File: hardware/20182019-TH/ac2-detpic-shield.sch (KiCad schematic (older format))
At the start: 46 parts, among them J1 HEADER, J2 HEADER, J3 HEADER, J4 HEADER, J5 HEADER, J6 HEADER, J7 HEADER, Q1 VN2222, Q2 VN2222, SW1 SW_DIP_x04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

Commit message: fixed bug in J3 header in 20182019-TH pcb
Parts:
- removed J3: HEADER, Connector_PinHeader_2.54mm:PinHeader_1x07_P2.54mm_Vertical, symbol Connector:Conn_01x07_Male
- added J3: HEADER, Connector_PinHeader_2.54mm:PinHeader_1x06_P2.54mm_Vertical, symbol Connector:Conn_01x06_Male
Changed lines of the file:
@@
 Text Label 1450 2950 0    50   ~ 10
 RD0
-Text Label 1450 3150 0    50   ~ 10
+Text Label 1550 3150 0    50   ~ 10
 RD10
 Text Label 1600 3250 0    50   ~ 10
@@
 $EndComp
 $Comp
-L Connector:Conn_01x07_Male J3
-U 1 1 5C9D88C9
-P 1750 2850
-F 0 "J3" H 1650 2850 50  0000 R CNN
-F 1 "HEADER" V 1700 3000 50  0000 R CNN
-F 2 "Connector_PinHeader_2.54mm:PinHeader_1x07_P2.54mm_Vertical" H 1750 2850 50  0001 C CNN
-F 3 "~" H 1750 2850 50  0001 C CNN
-	1    1750 2850
-	-1   0    0    1
-$EndComp
-$Comp
 L Connector:Conn_01x02_Male J4
 U 1 1 5C9DA65B
@@
 	1550 3050 1450 3050
 Wire Wire Line
-	1550 3150 1450 3150
-Wire Wire Line
 	1550 3350 1450 3350
 Wire Wire Line
@@
 Text Notes 10570 7640 0    50   ~ 10
 v1.1 May 2019
+$Comp
+L Connector:Conn_01x06_Male J3
+U 1 1 5CF092BF
+P 1750 2850
+F 0 "J3" H 1650 2800 50  0000 R CNN
+F 1 "HEADER" V 1700 2950 50  0000 R CNN
+F 2 "Connector_PinHeader_2.54mm:PinHeader_1x06_P2.54mm_Vertical" H 1750 2850 50  0001 C CNN
+F 3 "~" H 1750 2850 50  0001 C CNN
+	1    1750 2850
+	-1   0    0    1
+$EndComp
+Wire Wire Line
+	1450 3150 1750 3150
 $EndSCHEMATC

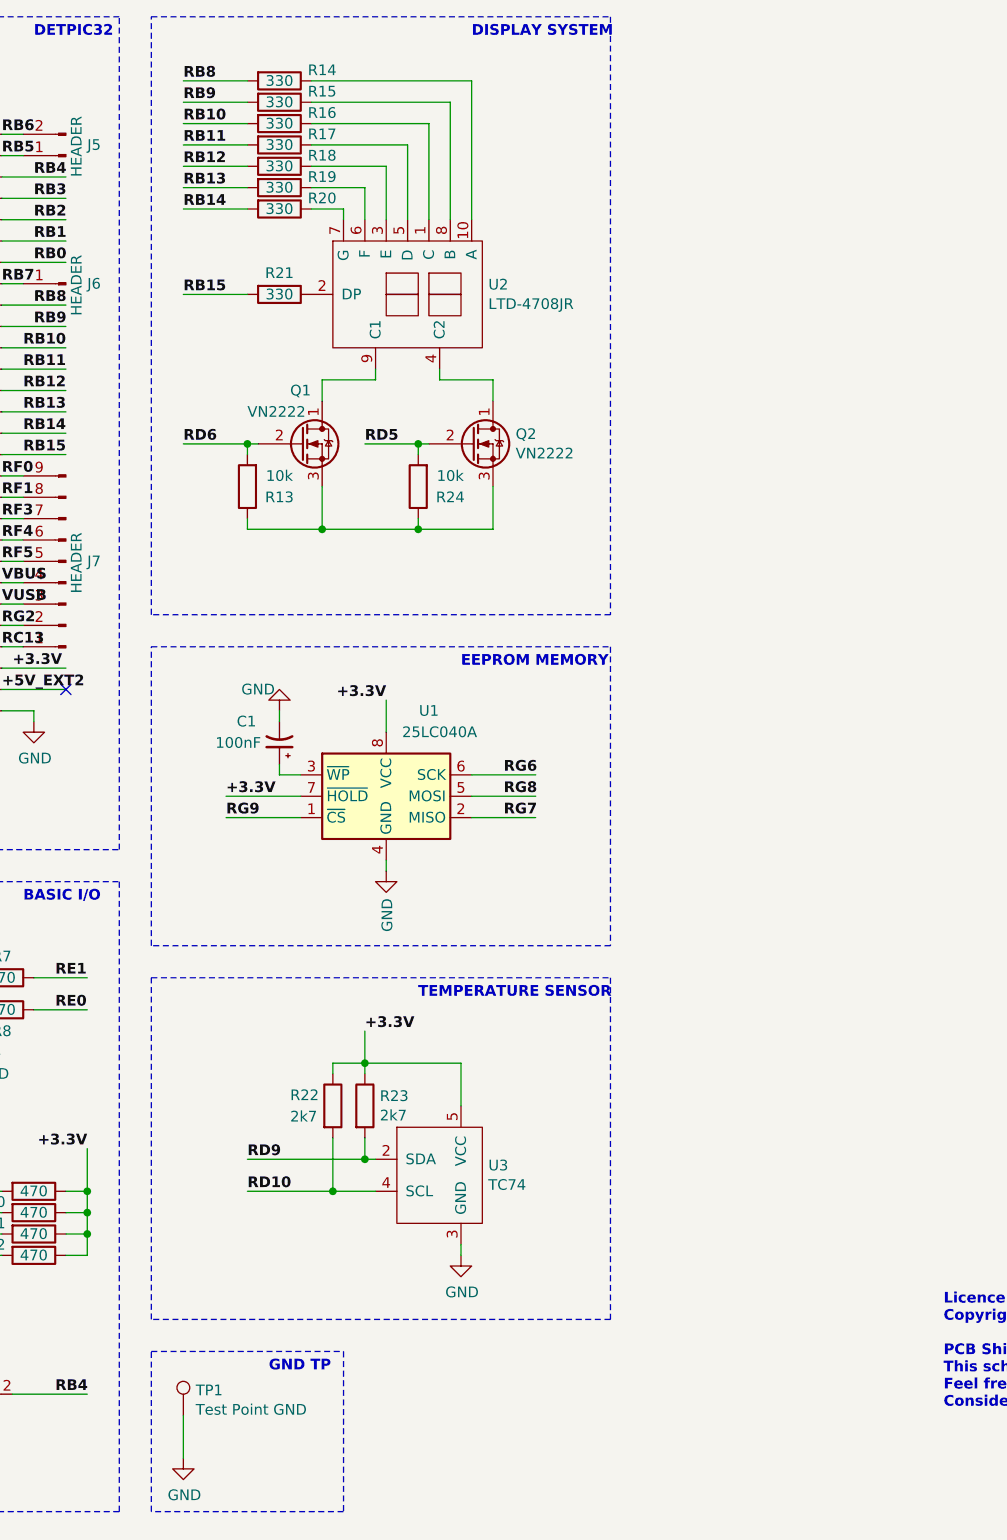
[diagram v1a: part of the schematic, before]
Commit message: rotary pot, option on dual single 7seg displays and fix in trim pot
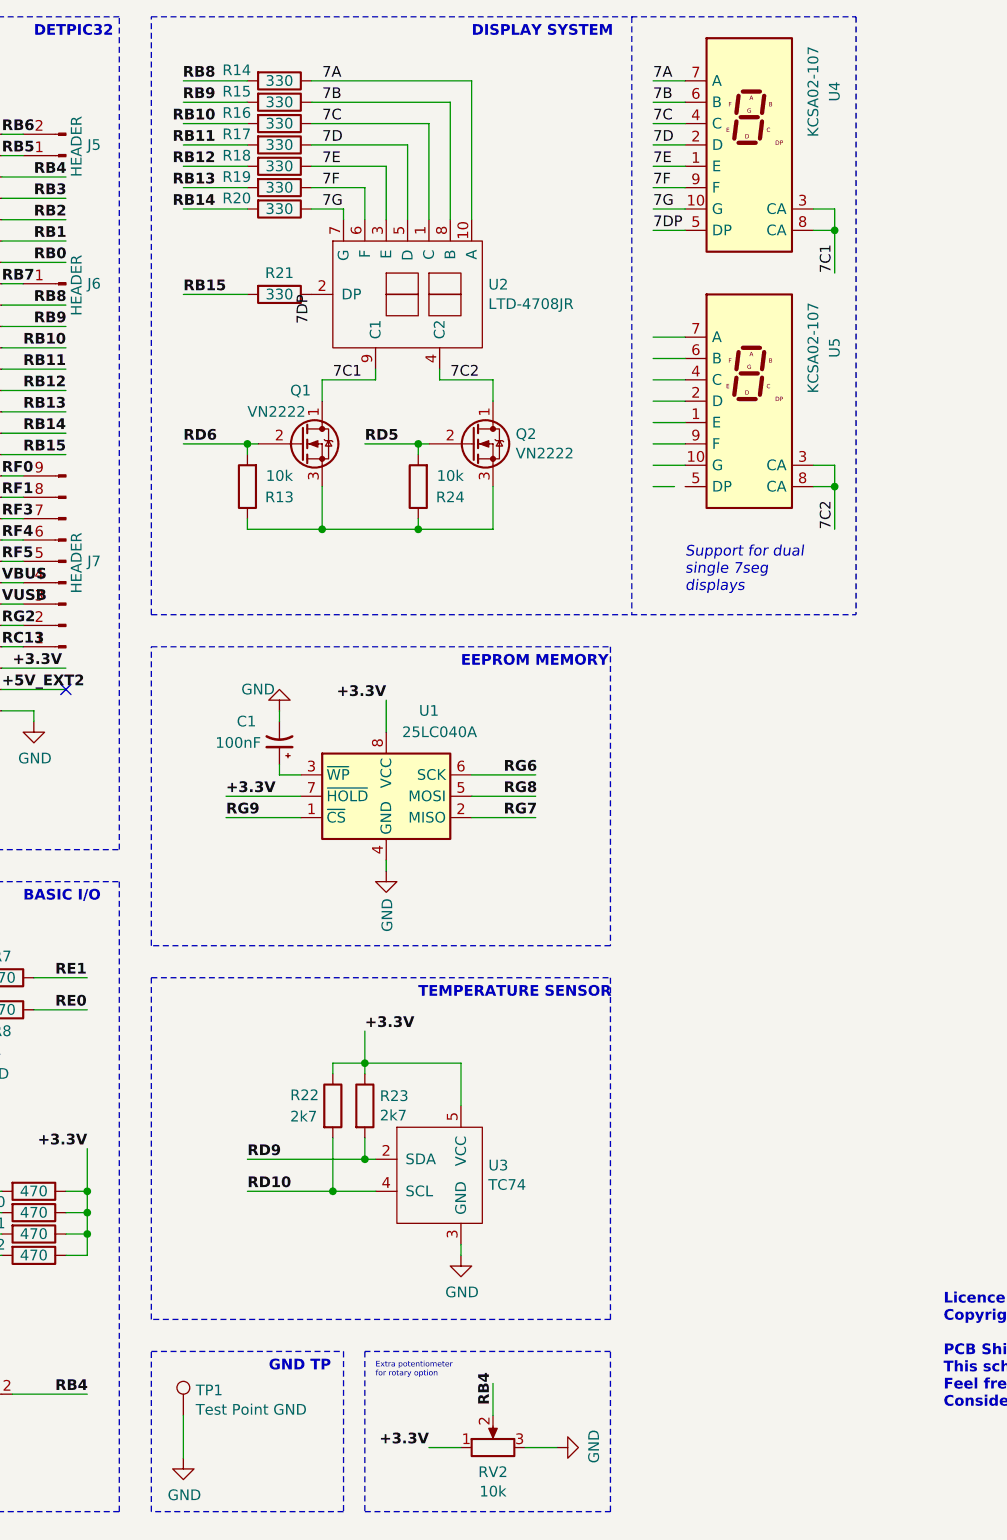
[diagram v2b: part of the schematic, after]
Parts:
- added RV2: 10k, Potentiometer_THT:Potentiometer_Piher_T-16H_Single_Horizontal, symbol Device:R_POT
- added U4, U5: KCSA02-107, Display_7Segment:7SegmentLED_LTS6760_LTS6780, symbol Display_Character:KCSA02-107
- RV1: footprint Potentiometer_THT:Potentiometer_ACP_CA14V-15_Vertical -> Potentiometer_THT:Potentiometer_ACP_CA9-V10_Vertical
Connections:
- net labels added: 7A, 7B, 7C, 7C1, 7C2, 7D, 7DP, 7E, 7F, 7G
- wire segments 172 -> 199
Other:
- note added: "Extra potentiometer\nfor rotary option"
- note added: "Support for dual \nsingle 7seg\ndisplays"
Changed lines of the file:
@@
 Wire Wire Line
 	3750 1500 3450 1500
-Text Label 3450 900  0    50   ~ 10
+Text Label 3600 900  2    50   ~ 10
 RB8
-Text Label 3450 1000 0    50   ~ 10
+Text Label 3600 1000 2    50   ~ 10
 RB9
-Text Label 3450 1100 0    50   ~ 10
+Text Label 3600 1100 2    50   ~ 10
 RB10
-Text Label 3450 1200 0    50   ~ 10
+Text Label 3600 1200 2    50   ~ 10
 RB11
-Text Label 3450 1300 0    50   ~ 10
+Text Label 3600 1300 2    50   ~ 10
 RB12
-Text Label 3450 1400 0    50   ~ 10
+Text Label 3600 1400 2    50   ~ 10
 RB13
-Text Label 3450 1500 0    50   ~ 10
+Text Label 3600 1500 2    50   ~ 10
 RB14
 $Comp
@@
 	4800 900  4800 1550
 Wire Wire Line
-	3750 1900 3450 1900
-Text Label 3450 1900 0    50   ~ 10
-RB15
-Wire Wire Line
 	4350 2250 4350 2300
 Wire Wire Line
@@
 	4550 2600 4300 2600
 Wire Notes Line
-	3300 600  5450 600
-Wire Notes Line
-	5450 600  5450 3400
-Wire Notes Line
-	5450 3400 3300 3400
+	5550 600  5550 3400
 Wire Notes Line
 	3300 3400 3300 600
@@
 F 0 "RV1" H 2430 7096 50  0000 R CNN
 F 1 "10k" H 2430 7005 50  0000 R CNN
-F 2 "Potentiometer_THT:Potentiometer_ACP_CA14V-15_Vertical" H 2500 7050 50  0001 C CNN
+F 2 "Potentiometer_THT:Potentiometer_ACP_CA9-V10_Vertical" H 2500 7050 50  0001 C CNN
 F 3 "~" H 2500 7050 50  0001 C CNN
 	1    2500 7050
@@
 U 1 1 5CA1D1A8
 P 3900 900
-F 0 "R14" V 3850 1100 50  0000 C CNN
+F 0 "R14" V 3850 700 50  0000 C CNN
 F 1 "330" V 3900 900 50  0000 C CNN
 F 2 "Resistor_THT:R_Axial_DIN0207_L6.3mm_D2.5mm_P7.62mm_Horizontal" V 3830 900 50  0001 C CNN
@@
 U 1 1 5CA1F029
 P 3900 1000
-F 0 "R15" V 3850 1200 50  0000 C CNN
+F 0 "R15" V 3850 800 50  0000 C CNN
 F 1 "330" V 3900 1000 50  0000 C CNN
 F 2 "Resistor_THT:R_Axial_DIN0207_L6.3mm_D2.5mm_P7.62mm_Horizontal" V 3830 1000 50  0001 C CNN
@@
 U 1 1 5CA25E86
 P 3900 1100
-F 0 "R16" V 3850 1300 50  0000 C CNN
+F 0 "R16" V 3850 900 50  0000 C CNN
 F 1 "330" V 3900 1100 50  0000 C CNN
 F 2 "Resistor_THT:R_Axial_DIN0207_L6.3mm_D2.5mm_P7.62mm_Horizontal" V 3830 1100 50  0001 C CNN
@@
 U 1 1 5CA2CC58
 P 3900 1200
-F 0 "R17" V 3850 1400 50  0000 C CNN
+F 0 "R17" V 3850 1000 50  0000 C CNN
 F 1 "330" V 3900 1200 50  0000 C CNN
 F 2 "Resistor_THT:R_Axial_DIN0207_L6.3mm_D2.5mm_P7.62mm_Horizontal" V 3830 1200 50  0001 C CNN
@@
 U 1 1 5CA33A2A
 P 3900 1300
-F 0 "R18" V 3850 1500 50  0000 C CNN
+F 0 "R18" V 3850 1100 50  0000 C CNN
 F 1 "330" V 3900 1300 50  0000 C CNN
 F 2 "Resistor_THT:R_Axial_DIN0207_L6.3mm_D2.5mm_P7.62mm_Horizontal" V 3830 1300 50  0001 C CNN
@@
 U 1 1 5CA41AE3
 P 3900 1400
-F 0 "R19" V 3850 1600 50  0000 C CNN
+F 0 "R19" V 3850 1200 50  0000 C CNN
 F 1 "330" V 3900 1400 50  0000 C CNN
 F 2 "Resistor_THT:R_Axial_DIN0207_L6.3mm_D2.5mm_P7.62mm_Horizontal" V 3830 1400 50  0001 C CNN
@@
 U 1 1 5CA488AB
 P 3900 1500
-F 0 "R20" V 3850 1700 50  0000 C CNN
+F 0 "R20" V 3850 1300 50  0000 C CNN
 F 1 "330" V 3900 1500 50  0000 C CNN
 F 2 "Resistor_THT:R_Axial_DIN0207_L6.3mm_D2.5mm_P7.62mm_Horizontal" V 3830 1500 50  0001 C CNN
@@
 	4100 3000 4550 3000
 $Comp
-L Device:R R21
-U 1 1 5CA72E7A
-P 3900 1900
-F 0 "R21" V 3800 1900 50  0000 C CNN
-F 1 "330" V 3900 1900 50  0000 C CNN
-F 2 "Resistor_THT:R_Axial_DIN0207_L6.3mm_D2.5mm_P7.62mm_Horizontal" V 3830 1900 50  0001 C CNN
-F 3 "~" H 3900 1900 50  0001 C CNN
-	1    3900 1900
-	0    1    1    0
-$EndComp
-$Comp
 L Memory_EEPROM:25LCxxx U1
 U 1 1 5C985584
@@
 Wire Wire Line
 	1450 3150 1750 3150
+$Comp
+L Display_Character:KCSA02-107 U4
+U 1 1 5E60EA09
+P 6100 1200
+F 0 "U4" V 6500 1450 50  0000 C CNN
+F 1 "KCSA02-107" V 6400 1450 50  0000 C CNN
+F 2 "Display_7Segment:7SegmentLED_LTS6760_LTS6780" H 6100 600 50  0001 C CNN
+F 3 "http://www.kingbright.com/attachments/file/psearch/000/00/00/KCSA02-107(Ver.10A).pdf" H 5600 1675 50  0001 L CNN
+	1    6100 1200
+	1    0    0    -1
+$EndComp
+$Comp
+L Display_Character:KCSA02-107 U5
+U 1 1 5E63DD93
+P 6100 2400
+F 0 "U5" V 6500 2650 50  0000 C CNN
+F 1 "KCSA02-107" V 6400 2650 50  0000 C CNN
+F 2 "Display_7Segment:7SegmentLED_LTS6760_LTS6780" H 6100 1800 50  0001 C CNN
+F 3 "http://www.kingbright.com/attachments/file/psearch/000/00/00/KCSA02-107(Ver.10A).pdf" H 5600 2875 50  0001 L CNN
+	1    6100 2400
+	1    0    0    -1
+$EndComp
+Wire Notes Line
+	6600 600  6600 3400
+Wire Notes Line
+	3300 600  6600 600
+Wire Notes Line
+	3300 3400 6600 3400
+Text Notes 5800 3300 0    50   Italic 0
+Support for dual \nsingle 7seg\ndisplays
+Text Label 4100 1500 0    50   ~ 0
+7G
+Text Label 4100 1400 0    50   ~ 0
+7F
+Text Label 4100 1300 0    50   ~ 0
+7E
+Text Label 4100 1200 0    50   ~ 0
+7D
+Text Label 4100 1100 0    50   ~ 0
+7C
+Text Label 4100 1000 0    50   ~ 0
+7B
+Text Label 4100 900  0    50   ~ 0
+7A
+Wire Wire Line
+	3750 1900 3450 1900
+Text Label 3450 1900 0    50   ~ 10
+RB15
+$Comp
+L Device:R R21
+U 1 1 5CA72E7A
+P 3900 1900
+F 0 "R21" V 3800 1900 50  0000 C CNN
+F 1 "330" V 3900 1900 50  0000 C CNN
+F 2 "Resistor_THT:R_Axial_DIN0207_L6.3mm_D2.5mm_P7.62mm_Horizontal" V 3830 1900 50  0001 C CNN
+F 3 "~" H 3900 1900 50  0001 C CNN
+	1    3900 1900
+	0    1    1    0
+$EndComp
+Text Label 4050 1900 3    50   ~ 0
+7DP
+Text Label 4150 2300 0    50   ~ 0
+7C1
+Text Label 4700 2300 0    50   ~ 0
+7C2
+Wire Wire Line
+	5800 1000 5650 1000
+Wire Wire Line
+	5800 900  5650 900
+Wire Wire Line
+	5800 1100 5650 1100
+Wire Wire Line
+	5800 1200 5650 1200
+Wire Wire Line
+	5800 1300 5650 1300
+Wire Wire Line
+	5800 1400 5650 1400
+Wire Wire Line
+	5800 1500 5650 1500
+Wire Wire Line
+	5800 1600 5650 1600
+Wire Wire Line
+	6400 1500 6500 1500
+Wire Wire Line
+	6500 1500 6500 1600
+Wire Wire Line
+	6400 1600 6500 1600
+Connection ~ 6500 1600
+Wire Wire Line
+	6500 1600 6500 1800
+Wire Wire Line
+	5800 2100 5650 2100
+Wire Wire Line
+	5800 2200 5650 2200
+Wire Wire Line
+	5800 2300 5650 2300
+Wire Wire Line
+	5800 2400 5650 2400
+Wire Wire Line
+	5800 2500 5650 2500
+Wire Wire Line
+	5800 2600 5650 2600
+Wire Wire Line
+	5800 2700 5650 2700
+Wire Wire Line
+	5750 2800 5650 2800
+Wire Wire Line
+	6400 2700 6500 2700
+Wire Wire Line
+	6500 2700 6500 2800
+Wire Wire Line
+	6400 2800 6500 2800
+Connection ~ 6500 2800
+Wire Wire Line
+	6500 2800 6500 3000
+Text Label 5650 900  0    50   ~ 0
+7A
+Text Label 5650 1000 0    50   ~ 0
+7B
+Text Label 5650 1100 0    50   ~ 0
+7C
+Text Label 5650 1200 0    50   ~ 0
+7D
+Text Label 5650 1300 0    50   ~ 0
+7E
+Text Label 5650 1400 0    50   ~ 0
+7F
+Text Label 5650 1500 0    50   ~ 0
+7G
+Text Label 5650 1600 0    50   ~ 0
+7DP
+Text Label 6500 1800 1    50   ~ 0
+7C1
+Text Label 6500 3000 1    50   ~ 0
+7C2
+$Comp
+L Device:R_POT RV2
+U 1 1 5E854091
+P 4900 7300
+F 0 "RV2" V 4785 7300 50  0000 C CNN
+F 1 "10k" V 4694 7300 50  0000 C CNN
+F 2 "Potentiometer_THT:Potentiometer_Piher_T-16H_Single_Horizontal" H 4900 7300 50  0001 C CNN
+F 3 "~" H 4900 7300 50  0001 C CNN
+	1    4900 7300
+	0    -1   -1   0
+$EndComp
+Wire Wire Line
+	4900 7150 4900 7000
+Wire Wire Line
+	5050 7300 5200 7300
+Wire Wire Line
+	4750 7300 4600 7300
+Text Label 4900 7100 1    50   ~ 10
+RB4
+$Comp
+L power:GND #PWR05
+U 1 1 5E87CB07
+P 5200 7300
+F 0 "#PWR05" H 5200 7050 50  0001 C CNN
+F 1 "GND" H 5205 7127 50  0000 C CNN
+F 2 "" H 5200 7300 50  0001 C CNN
+F 3 "" H 5200 7300 50  0001 C CNN
+	1    5200 7300
+	0    -1   -1   0
+$EndComp
+Text Label 4600 7300 2    50   ~ 10
++3.3V
+Wire Notes Line
+	4300 6850 4300 7600
+Wire Notes Line
+	4300 7600 5450 7600
+Wire Notes Line
+	5450 7600 5450 6850
+Wire Notes Line
+	5450 6850 4300 6850
+Text Notes 4350 6975 0    26   ~ 0
+Extra potentiometer\nfor rotary option
 $EndSCHEMATC

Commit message: changes docs of detpic to common directory + changes in the pcb and footprint (rotary pot)
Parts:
- RV2: footprint Potentiometer_THT:Potentiometer_Piher_T-16H_Single_Horizontal -> Potentiometer_THT:Potentiometer_Alps_RK163_Single_Horizontal
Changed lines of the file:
@@
 F 0 "RV2" V 4785 7300 50  0000 C CNN
 F 1 "10k" V 4694 7300 50  0000 C CNN
-F 2 "Potentiometer_THT:Potentiometer_Piher_T-16H_Single_Horizontal" H 4900 7300 50  0001 C CNN
+F 2 "Potentiometer_THT:Potentiometer_Alps_RK163_Single_Horizontal" H 4900 7300 50  0001 C CNN
 F 3 "~" H 4900 7300 50  0001 C CNN
 	1    4900 7300

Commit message: added detpic32 circuitry to schematic
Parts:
- added C? (x2): 20pF, Capacitor_THT:CP_Radial_D7.5mm_P2.50mm, symbol Device:CP1_Small
- added C?: 10uF, Capacitor_THT:CP_Radial_D7.5mm_P2.50mm, symbol Device:CP1_Small
- added C? (x6): 0.1uF, Capacitor_THT:CP_Radial_D7.5mm_P2.50mm, symbol Device:CP1_Small
- added C? (x2): 4.7uF, Capacitor_THT:CP_Radial_D7.5mm_P2.50mm, symbol Device:CP1_Small
- added D? (x2): LED, symbol Device:LED
- added D?: D_Small, symbol Device:D_Small
- added R?: 4k7, Resistor_THT:R_Axial_DIN0207_L6.3mm_D2.5mm_P7.62mm_Horizontal, symbol Device:R
- added R? (x2): 330, Resistor_THT:R_Axial_DIN0207_L6.3mm_D2.5mm_P7.62mm_Horizontal, symbol Device:R
- added SW?: SW_Push, symbol Switch:SW_Push
- added U?: PIC32MX795F512H-80V_PT, TQFP64_10X10MC, symbol PIC32MX795F512H-80V_PT:PIC32MX795F512H-80V_PT
- added U?: TC1262-33, symbol Regulator_Linear:TC1262-33
- added U?: MM232R, FTDI_MM232R, symbol MM232R:MM232R
- added Y?: 8MHz, symbol Device:Crystal_Small
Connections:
- net labels added: +5V_EXT, +5V_USB, RC12, RC15, U1_RX, U1_TX, VCAP
- net labels removed: +5V_EXT1, +5V_EXT2
- wire segments 199 -> 328
- no-connect marks 2 -> 10
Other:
- note added: "An expensive one"
- note added: "FTID"
- note added: "POWER DELIVERY"
- note removed: "Licence: MIT\nCopyright 2019 Diogo Correia\n\nPCB Shield that extends the detpic32 development board created at DETI UA\nThis schematic is intended to be updated has the subject evolves\nFeel free to request changes or make them yourself\nConsider contributing your changes to the repo"
- moved on the sheet: C1, Q1, Q2, R13, R14, R15, R16, R17, R18, R19, R20, R21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

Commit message: added footprints, changes footprints and generated new net file
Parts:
- added J8: MPLAB ICD3, Connector_PinHeader_2.54mm:PinHeader_1x06_P2.54mm_Horizontal, symbol Connector:Conn_01x06_Female
- C1: footprint Capacitor_THT:CP_Radial_D7.5mm_P2.50mm -> Capacitor_THT:C_Disc_D6.0mm_W2.5mm_P5.00mm
- C10, C11, C12: renamed from C?; footprint Capacitor_THT:CP_Radial_D7.5mm_P2.50mm -> Capacitor_SMD:C_0201_0603Metric
- C2, C3, C4, C5, C6, C7, C8, C9: renamed from C?; footprint Capacitor_THT:CP_Radial_D7.5mm_P2.50mm -> Capacitor_SMD:C_0805_2012Metric_Pad1.15x1.40mm_HandSolder
- D5, D6, D7: renamed from D?; footprint (none) -> LED_SMD:LED_0603_1608Metric
- R1, R10, R11, R12, R13, R14, R15, R16, R17, R18, R19, R2, R20, R21, R22, R23, R24, R3, R4, R5, R6, R7, R8, R9: footprint Resistor_THT:R_Axial_DIN0207_L6.3mm_D2.5mm_P7.62mm_Horizontal -> Resistor_SMD:R_0805_2012Metric_Pad1.15x1.40mm_HandSolder
- R25, R26, R27: renamed from R?; footprint Resistor_THT:R_Axial_DIN0207_L6.3mm_D2.5mm_P7.62mm_Horizontal -> Resistor_SMD:R_0805_2012Metric_Pad1.15x1.40mm_HandSolder
- SW2: renamed from SW?; footprint (none) -> Button_Switch_THT:SW_PUSH_6mm
- U6: renamed from U?; footprint TQFP64_10X10MC -> PIC32MX795F512H-80V_PT:TQFP64_10X10MC
- U7: renamed from U?; footprint (none) -> Package_TO_SOT_SMD:SOT-223
- U8: renamed from U?; footprint FTDI_MM232R -> MM232R:FTDI_MM232R
- Y1: renamed from Y?; footprint (none) -> Crystal:Crystal_HC49-4H_Vertical
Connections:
- net labels added: MCLR, PGC, PGD
- wire segments 328 -> 334
- no-connect marks 10 -> 9
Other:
- note added: "PROGRAMMING\nINTERFACES"
- moved on the sheet: C10, C11, C12, C2, C3, C4, C5, C6, C7, C8, C9, D5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

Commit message: small pcb organization of components
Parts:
- D5: footprint LED_SMD:LED_0603_1608Metric -> Diode_THT:D_A-405_P7.62mm_Horizontal
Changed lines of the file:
@@
 F 0 "D5" V 7300 5300 50  0000 R CNN
 F 1 "D_Small" V 7225 5500 50  0000 R CNN
-F 2 "LED_SMD:LED_0603_1608Metric" V 7225 5150 50  0001 C CNN
+F 2 "Diode_THT:D_A-405_P7.62mm_Horizontal" V 7225 5150 50  0001 C CNN
 F 3 "~" V 7225 5150 50  0001 C CNN
 	1    7225 5150

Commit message: some changes to pcb and footprints on pF caps to 0805
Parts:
- C10, C11, C12: footprint Capacitor_SMD:C_0201_0603Metric -> Capacitor_SMD:C_0805_2012Metric_Pad1.15x1.40mm_HandSolder
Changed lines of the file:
@@
 F 0 "C10" V 10925 3575 50  0000 R CNN
 F 1 "20pF" V 11000 3625 50  0000 R CNN
-F 2 "Capacitor_SMD:C_0201_0603Metric" H 10825 3525 50  0001 C CNN
+F 2 "Capacitor_SMD:C_0805_2012Metric_Pad1.15x1.40mm_HandSolder" H 10825 3525 50  0001 C CNN
 F 3 "~" H 10825 3525 50  0001 C CNN
 	1    10825 3525
@@
 F 0 "C11" V 10700 3950 50  0000 R CNN
 F 1 "20pF" V 10625 3975 50  0000 R CNN
-F 2 "Capacitor_SMD:C_0201_0603Metric" H 10825 3900 50  0001 C CNN
+F 2 "Capacitor_SMD:C_0805_2012Metric_Pad1.15x1.40mm_HandSolder" H 10825 3900 50  0001 C CNN
 F 3 "~" H 10825 3900 50  0001 C CNN
 	1    10825 3900
@@
 F 0 "C12" H 10925 2125 50  0000 R CNN
 F 1 "0.1uF" H 11025 2050 50  0000 R CNN
-F 2 "Capacitor_SMD:C_0201_0603Metric" H 11025 2125 50  0001 C CNN
+F 2 "Capacitor_SMD:C_0805_2012Metric_Pad1.15x1.40mm_HandSolder" H 11025 2125 50  0001 C CNN
 F 3 "~" H 11025 2125 50  0001 C CNN
 	1    11025 2125
